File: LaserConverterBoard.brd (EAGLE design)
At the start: 84.3 x 66.5 mm, 46 parts, among them J10 FAN, J11 E-STOP, J2 Z-STOP, J3 Y, J4 X, J5 04-JST-B4B-XH-A, J6 04-JST-B4B-XH-A, J7 04-JST-B4B-XH-A, J9 AIR, Q1 FDN5630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

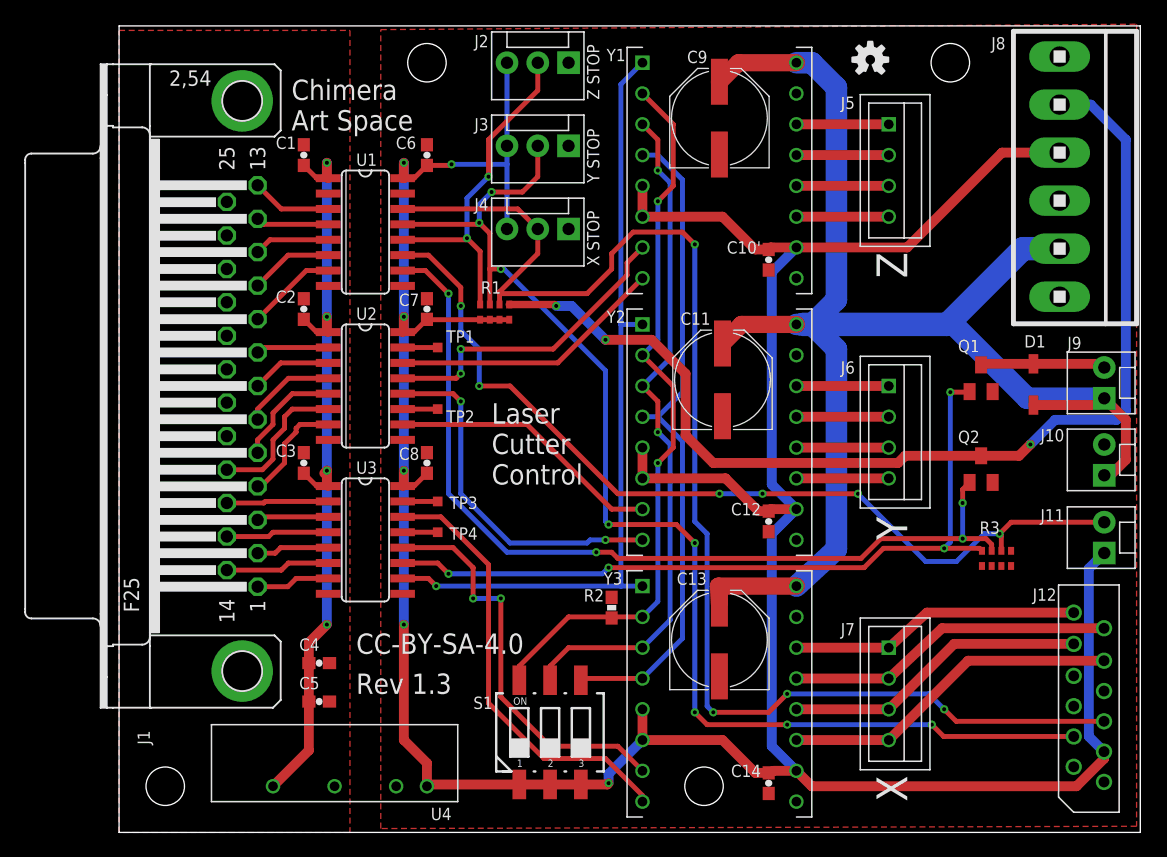
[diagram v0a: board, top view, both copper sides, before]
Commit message: More silkscreen and plug fixes to full-size board
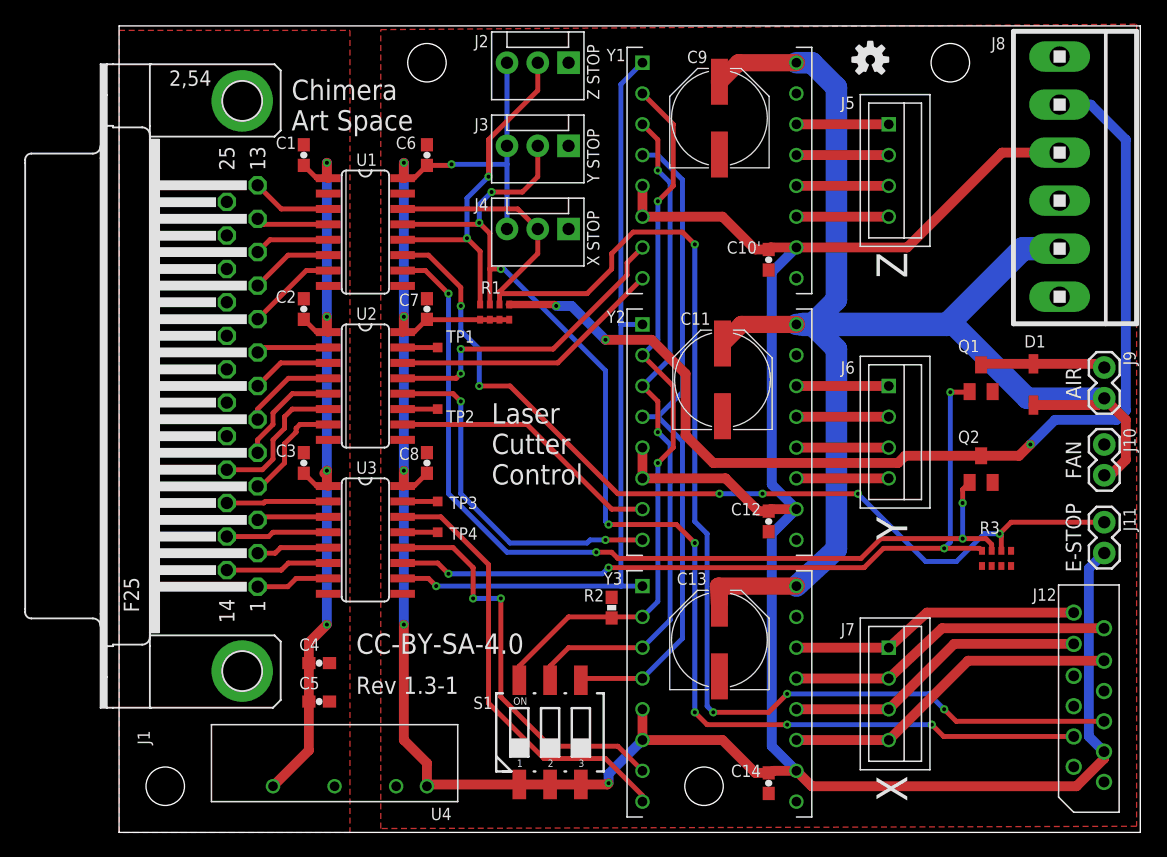
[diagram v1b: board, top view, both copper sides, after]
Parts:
- J10, J11, J9: device SparkFun-Connectors:MOLEX-1X2 -> SparkFun-Connectors:1X02
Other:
- board text added: "Rev 1.3-1"
- board text removed: "J10"
- board text removed: "J11"
- board text removed: "J9"
- board text removed: "Rev 1.3"
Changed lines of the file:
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@@
 <text x="30.48" y="58.928" size="1.016" layer="21" font="vector" rot="R180">J3</text>
 <text x="30.48" y="52.324" size="1.016" layer="21" font="vector" rot="R180">J4</text>
-<text x="78.232" y="39.878" size="1.016" layer="21" font="vector">J9</text>
-<text x="77.978" y="33.274" size="1.016" layer="21" font="vector" rot="R180">J10</text>
-<text x="77.978" y="26.67" size="1.016" layer="21" font="vector" rot="R180">J11</text>
 <text x="14.224" y="57.912" size="1.6764" layer="21" font="vector" ratio="15">Chimera
 Art Space</text>
@@
 Control</text>
 <text x="19.558" y="14.732" size="1.6764" layer="21" font="vector" ratio="15">CC-BY-SA-4.0</text>
-<text x="19.558" y="11.43" size="1.6764" layer="21" font="vector" ratio="15">Rev 1.3</text>
+<text x="19.558" y="11.43" size="1.4224" layer="21" font="vector" ratio="15">Rev 1.3-1</text>
 <text x="17.018" y="12.192" size="1.6764" layer="22" font="fixed" ratio="15" rot="MR90">S1 = microstep select
 MS1   MS2   MS3
@@
 <attribute name="VALUE" x="32.893" y="41.656" size="1.27" layer="27" ratio="10" rot="R180" display="off"/>
 </element>
-<element name="J11" library="SparkFun-Connectors" package="MOLEX-1X2" value="E-STOP" x="81.28" y="23.0505" locked="yes" rot="R90"/>
-<element name="J10" library="SparkFun-Connectors" package="MOLEX-1X2" value="FAN" x="81.28" y="29.464" locked="yes" rot="R90"/>
+<element name="J11" library="SparkFun-Connectors" package="1X02" value="E-STOP" x="81.28" y="23.0505" locked="yes" smashed="yes" rot="R90">
+<attribute name="NAME" x="82.8548" y="26.8097" size="1.016" layer="25" font="vector" ratio="10" rot="R270"/>
+<attribute name="VALUE" x="79.375" y="24.3205" size="1.27" layer="21" font="vector" ratio="15" rot="R90" align="bottom-center"/>
+</element>
+<element name="J10" library="SparkFun-Connectors" package="1X02" value="FAN" x="81.28" y="29.464" locked="yes" smashed="yes" rot="R90">
+<attribute name="NAME" x="82.8548" y="33.3502" size="1.016" layer="25" font="vector" ratio="12" rot="R270"/>
+<attribute name="VALUE" x="79.375" y="30.734" size="1.27" layer="21" font="vector" ratio="15" rot="R90" align="bottom-center"/>
+</element>
 <element name="Y3" library="pololu" package="POLOLU_STEPPER_DRIVER" value="POLOLU_A4988" x="49.53" y="11.43" locked="yes" smashed="yes">
 <attribute name="NAME" x="41.529" y="21.463" size="1.016" layer="21" font="vector" rot="R180"/>
@@
 <attribute name="VALUE" x="59.69" y="58.42" size="1.27" layer="21" rot="R270" display="off"/>
 </element>
-<element name="J9" library="SparkFun-Connectors" package="MOLEX-1X2" value="AIR" x="81.28" y="35.814" locked="yes" rot="R90"/>
+<element name="J9" library="SparkFun-Connectors" package="1X02" value="AIR" x="81.28" y="35.814" locked="yes" smashed="yes" rot="R90">
+<attribute name="NAME" x="82.8548" y="39.7002" size="1.016" layer="25" font="vector" ratio="12" rot="R270"/>
+<attribute name="VALUE" x="79.375" y="37.084" size="1.27" layer="21" font="vector" ratio="15" rot="R90" align="bottom-center"/>
+</element>
 <element name="D1" library="semicon-smd-ipc" package="SOD123" value="" x="75.438" y="36.957" locked="yes" smashed="yes" rot="R90">
 <attribute name="NAME" x="74.676" y="40.005" size="1.016" layer="25" font="vector"/>

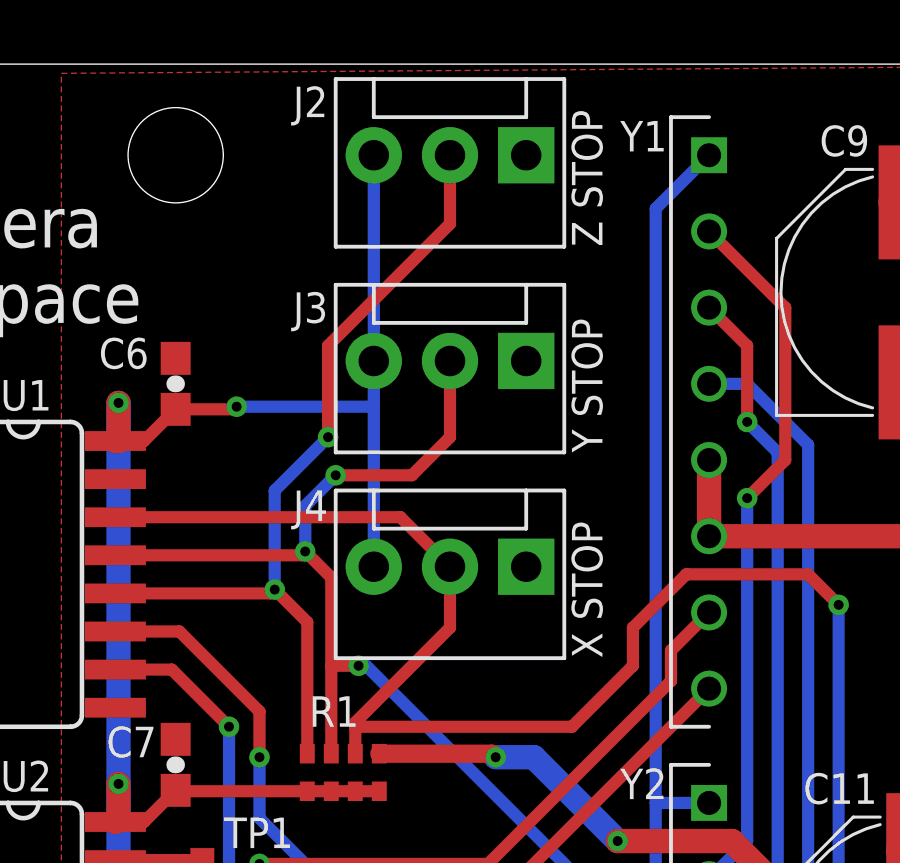
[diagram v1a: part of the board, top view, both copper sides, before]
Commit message: More tweaks to 1.3-1 and 1.3b, some repositioning and swapping of parts for layout, now that I've seen what the inside of the laser cutter looks like. Added pinouts for X and Y limits to the simple board, and just now realize I might have problems with the digital isolators being one way only...
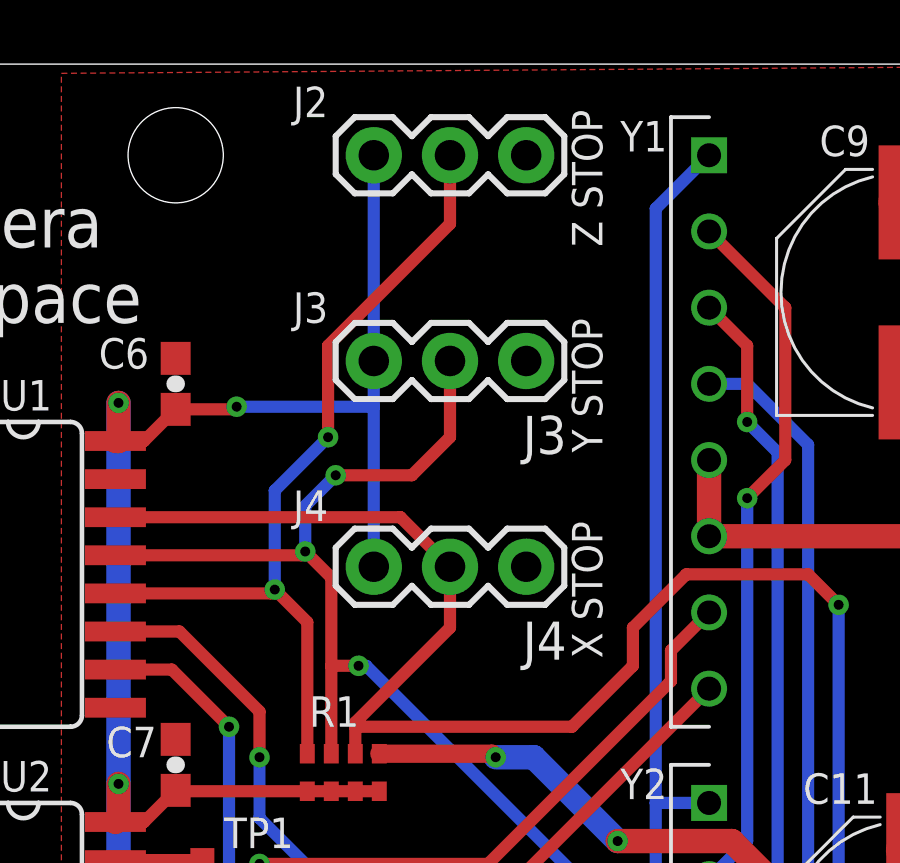
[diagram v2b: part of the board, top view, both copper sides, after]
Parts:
- J2, J3, J4: device SparkFun-Connectors:MOLEX-1X3 -> SparkFun-Connectors:1X03
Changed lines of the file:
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@@
 <layer number="19" name="Unrouted" color="6" fill="1" visible="yes" active="yes"/>
 <layer number="20" name="Dimension" color="15" fill="1" visible="yes" active="yes"/>
-<layer number="21" name="tPlace" color="7" fill="1" visible="yes" active="yes"/>
+<layer number="21" name="tPlace" color="15" fill="1" visible="yes" active="yes"/>
 <layer number="22" name="bPlace" color="7" fill="1" visible="yes" active="yes"/>
 <layer number="23" name="tOrigins" color="15" fill="1" visible="yes" active="yes"/>
@@
 <layer number="27" name="tValues" color="7" fill="1" visible="yes" active="yes"/>
 <layer number="28" name="bValues" color="7" fill="1" visible="yes" active="yes"/>
-<layer number="29" name="tStop" color="7" fill="3" visible="yes" active="yes"/>
-<layer number="30" name="bStop" color="7" fill="6" visible="yes" active="yes"/>
-<layer number="31" name="tCream" color="7" fill="4" visible="yes" active="yes"/>
-<layer number="32" name="bCream" color="7" fill="5" visible="yes" active="yes"/>
-<layer number="33" name="tFinish" color="6" fill="3" visible="yes" active="yes"/>
-<layer number="34" name="bFinish" color="6" fill="6" visible="yes" active="yes"/>
-<layer number="35" name="tGlue" color="7" fill="4" visible="yes" active="yes"/>
-<layer number="36" name="bGlue" color="7" fill="5" visible="yes" active="yes"/>
+<layer number="29" name="tStop" color="7" fill="3" visible="no" active="yes"/>
+<layer number="30" name="bStop" color="7" fill="6" visible="no" active="yes"/>
+<layer number="31" name="tCream" color="7" fill="4" visible="no" active="yes"/>
+<layer number="32" name="bCream" color="7" fill="5" visible="no" active="yes"/>
+<layer number="33" name="tFinish" color="6" fill="3" visible="no" active="yes"/>
+<layer number="34" name="bFinish" color="6" fill="6" visible="no" active="yes"/>
+<layer number="35" name="tGlue" color="7" fill="4" visible="no" active="yes"/>
+<layer number="36" name="bGlue" color="7" fill="5" visible="no" active="yes"/>
 <layer number="37" name="tTest" color="7" fill="1" visible="yes" active="yes"/>
 <layer number="38" name="bTest" color="7" fill="1" visible="yes" active="yes"/>
@@
 </element>
 <element name="FRAME1" library="SparkFun-Aesthetics" package="CREATIVE_COMMONS" value="FRAME-LEDGER" x="24.13" y="-10.16"/>
-<element name="J4" library="SparkFun-Connectors" package="MOLEX-1X3" value="X" x="37.084" y="49.784" locked="yes" rot="R180"/>
-<element name="J3" library="SparkFun-Connectors" package="MOLEX-1X3" value="Y" x="37.084" y="56.642" locked="yes" rot="R180"/>
-<element name="J2" library="SparkFun-Connectors" package="MOLEX-1X3" value="Z-STOP" x="37.084" y="63.5" locked="yes" smashed="yes" rot="R180"/>
+<element name="J4" library="SparkFun-Connectors" package="1X03" value="X" x="37.084" y="49.784" locked="yes" rot="R180"/>
+<element name="J3" library="SparkFun-Connectors" package="1X03" value="Y" x="37.084" y="56.642" locked="yes" rot="R180"/>
+<element name="J2" library="SparkFun-Connectors" package="1X03" value="Z-STOP" x="37.084" y="63.5" locked="yes" smashed="yes" rot="R180"/>
 <element name="J7" library="con-jst-xh" package="B4B-XH" value="04-JST-B4B-XH-A" x="63.5" y="11.43" locked="yes" smashed="yes" rot="R270">
 <attribute name="NAME" x="60.706" y="17.272" size="1.016" layer="21" font="vector" rot="R180"/>

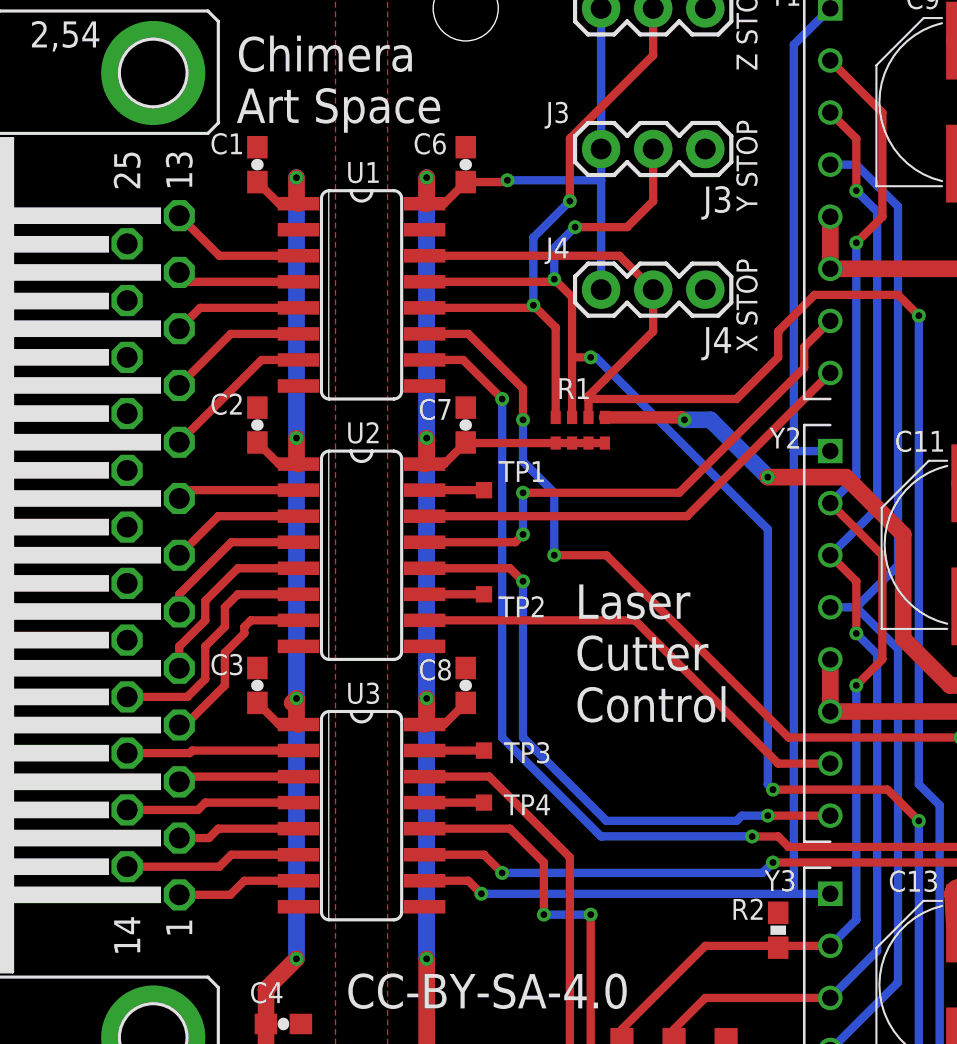
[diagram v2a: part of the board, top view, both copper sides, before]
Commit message: Okay, now the pins that need to feed back to the CNC controller actually can get there. What a mess. Bill of materials will now have three individual parts. I can see why Chris did it with nine Si8420's...
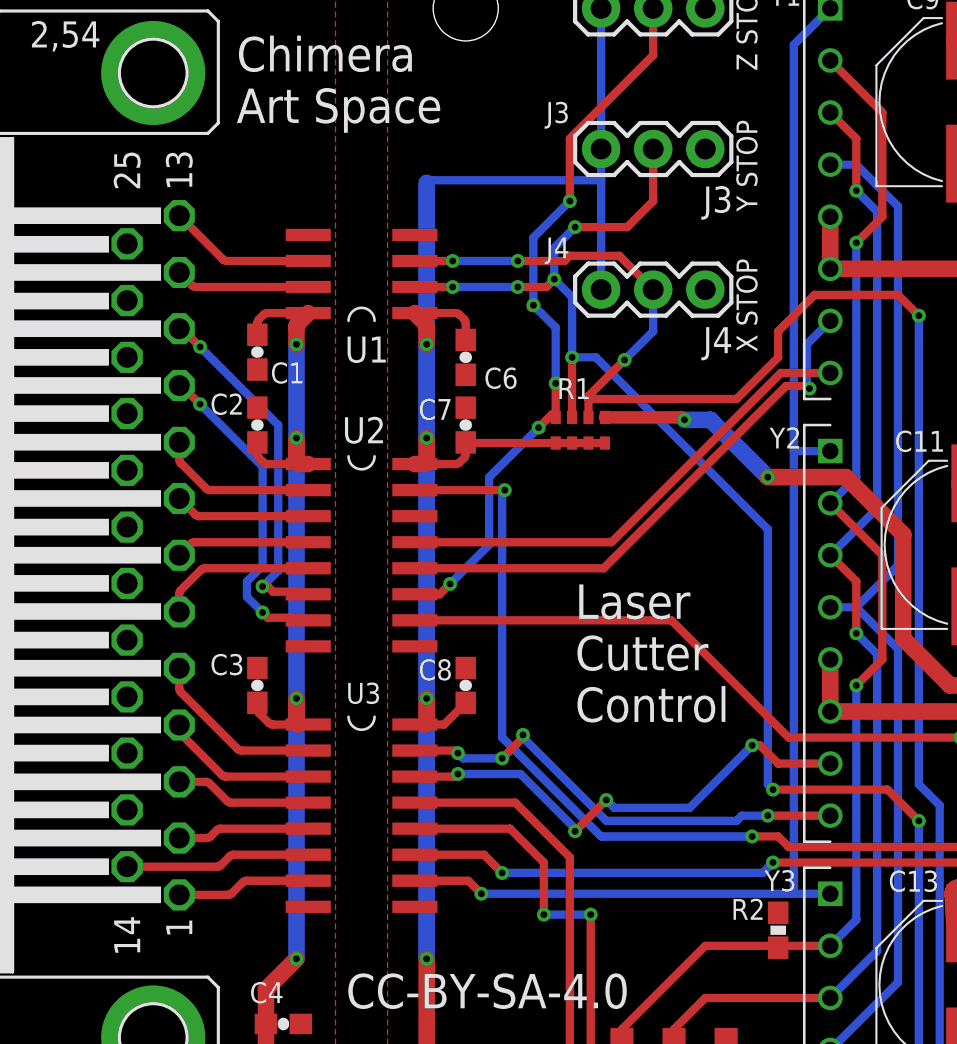
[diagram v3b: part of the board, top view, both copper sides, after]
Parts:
- removed TP1, TP2, TP3, TP4: TPTP08SQ, testpad:TP08SQ
- U1: value (none) -> SI8620IS; device silicon-labs:SO16 -> silicon-labs:SO08
- U2: value (none) -> SI8662IS1
- moved C6 9.40 mm to (25.4, 46.5), turned to 270 degrees
- moved C1 9.14 mm to (15.2, 46.7), turned to 270 degrees
- moved U1 1.02 mm to (20.3, 50.5), turned to 90 degrees
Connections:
- removed net AUX: J1.15, U3.4
- removed net AUX_ISO: TP4.TP, U3.13
- removed net OUT1: J1.16, U3.2
- removed net OUT1_ISO: TP3.TP, U3.15
- removed net OUT2: J1.17, U2.6
- removed net OUT2_ISO: TP2.TP, U2.11
- net ADIR: now also U2.2; no longer U1.7
- net ASTP: now also U2.3; no longer U2.2
- net ASTP_ISO: now also U2.14; no longer TP1.TP, U2.15
- net CNC_5V: now also U1.1; no longer U1.16
- net CNC_GND: now also U1.4; no longer U1.9
- net ESTOP: now also U2.7; no longer U1.6
- net ESTOP_ISO: now also U2.10; no longer U1.11
- net LASER_ISO: now also U2.15; no longer U1.10
- net PC_5V: now also U1.8; no longer U1.1
- net PC_GND: now also U1.5; no longer U1.8
- net XDIR: now also U3.4; no longer U3.3
- net XDIR_ISO: now also U3.13; no longer U3.14
- net XLIM: now also U1.6; no longer U1.3
- net XLIM_ISO: now also U1.3; no longer U1.14
- net YDIR: now also U3.2; no longer U2.5
- net YDIR_ISO: now also U3.15; no longer U2.12
- net YLIM: now also U1.7; no longer U1.4
- net YLIM_ISO: now also U1.2; no longer U1.13
- net YSTP: now also U3.3; no longer U2.7
- net YSTP_ISO: now also U3.14; no longer U2.10
- net ZDIR: now also U2.4; no longer U2.3
- net ZDIR_ISO: now also U2.13; no longer U2.14
- net ZLIM: now also U2.6; no longer U1.5
- net ZLIM_ISO: now also U2.11; no longer U1.12
- net ZSTP: now also U2.5; no longer U2.4
- net ZSTP_ISO: now also U2.12; no longer U2.13
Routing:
- net OUT2: track 11.9 -> 0.00 mm
- net ZLIM: track 6.24 -> 17.3 mm, vias 0 -> 2
- net ESTOP_ISO: track 75.0 -> 65.9 mm, vias 6 -> 4
- net ESTOP: track 6.86 -> 15.8 mm, vias 0 -> 2
- net AUX: track 8.50 -> 0.00 mm
- net OUT1: track 8.41 -> 0.00 mm
- net ZLIM_ISO: track 28.2 -> 35.5 mm, vias 2 -> 5
- net YDIR_ISO: track 29.5 -> 22.9 mm, vias 2 -> 4
- net PC_5V: track 64.8 -> 59.8 mm
- net CNC_5V: track 276.1 -> 281.1 mm, vias 6 -> 5
- net LASER_ISO: track 74.4 -> 69.9 mm
- net OUT2_ISO: track 2.90 -> 0.00 mm
- net OUT1_ISO: track 2.90 -> 0.00 mm
- net AUX_ISO: track 2.90 -> 0.00 mm
- net ASTP_ISO: track 2.90 -> 0.00 mm
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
